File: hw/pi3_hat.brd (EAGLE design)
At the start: 56.5 x 65 mm, 109 parts, among them J1 XT30P, J2 XT30P, U1 AP64351SO8EP, U10 CAT24C32SOIC8, U11 STM32G474CEU6, U12 TCAN334GSOT23, U13 TCAN334GSOT23, U2 DMMT5401, U3 DMG2305UX, U4 STM32G474CEU6, U5 TCAN334GSOT23, U6 TCAN334GSOT23, U7 STM32G474CEU6, U8 BMI088LGA16, U9 TCAN334GSOT23

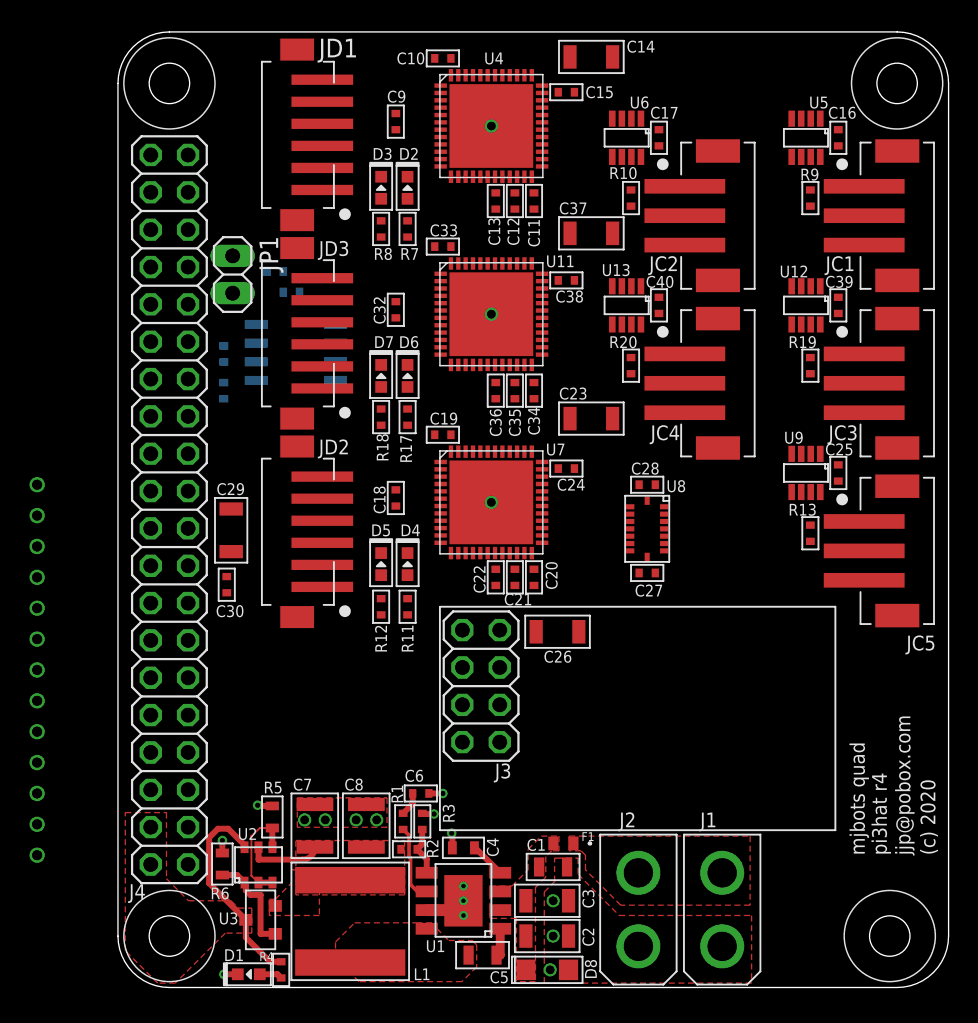
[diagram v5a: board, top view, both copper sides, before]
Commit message: Route all power and place all test points
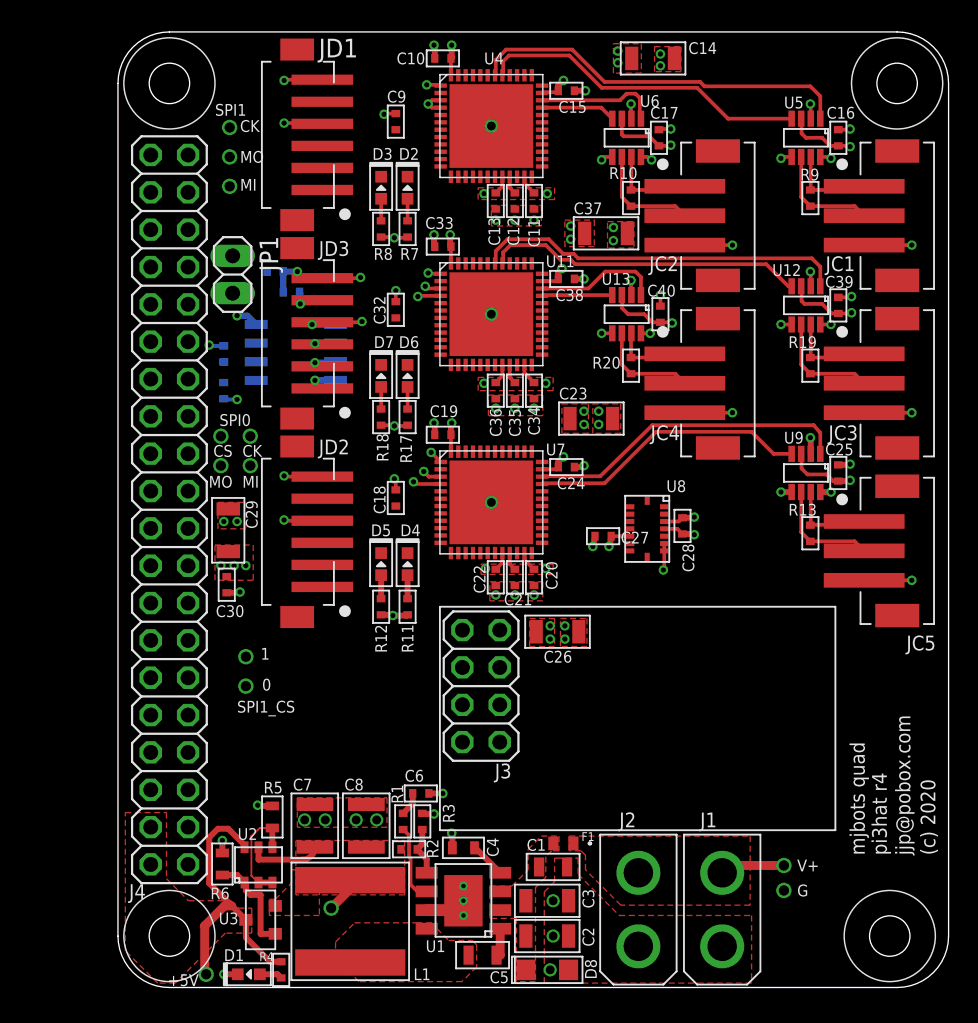
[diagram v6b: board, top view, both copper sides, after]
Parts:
- moved V+ 56.1 mm to (45.3, 8.30)
- moved GND 55.1 mm to (45.3, 6.60)
- moved SPI1_MOSI 41.2 mm to (7.60, 56.5)
- moved SPI1_SCLK 39.2 mm to (7.60, 58.5)
- moved SPI1_MISO 37.4 mm to (7.60, 54.5)
- moved REGOUT 35.1 mm to (14.5, 5.40)
- moved +5V 31.3 mm to (6.00, 0.90)
- moved SPI0_MOSI 29.3 mm to (7.00, 35.5)
- moved SPI0_MISO 28.4 mm to (9.00, 35.5)
- moved SPI0_SCLK 28.3 mm to (9.00, 37.5)
- moved SPI0_CS0 25.5 mm to (7.00, 37.5)
- moved SPI1_CS0 15.2 mm to (8.70, 20.5)
- moved SPI1_CS1 14.3 mm to (8.70, 22.5)
- moved C14 4.20 mm to (36.4, 63.2)
- moved C27 3.91 mm to (33.0, 30.7), turned to 180 degrees
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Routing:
- net +3V3: track 0.00 -> 76.9 mm, vias 0 -> 45
- net GND: track 8.48 -> 73.6 mm, vias 16 -> 84
- net N$18: track 0.00 -> 26.3 mm
- net N$42: track 0.00 -> 25.4 mm
- net N$17: track 0.00 -> 22.5 mm
- net N$55: track 0.00 -> 22.0 mm
- net N$41: track 0.00 -> 21.8 mm
- net N$54: track 0.00 -> 19.1 mm
- net N$40: track 0.00 -> 8.58 mm
- net N$100: track 0.00 -> 8.39 mm
- net N$8: track 0.00 -> 7.54 mm
- net N$46: track 0.00 -> 7.54 mm
- net N$4: track 0.00 -> 7.54 mm
- net N$25: track 0.00 -> 7.54 mm
- net N$27: track 0.00 -> 6.94 mm
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- added copper zone on layer 1, net +3V3
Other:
- board text added: "+5V"
- board text added: "0"
- board text added: "1"
- board text added: "CK"
- board text added: "CS"
- board text added: "G"
- board text added: "MI"
- board text added: "MO"
- board text added: "REGOUT"
- board text added: "SPI0"
- board text added: "SPI1"
- board text added: "SPI1_CS"
- board text added: "V+"

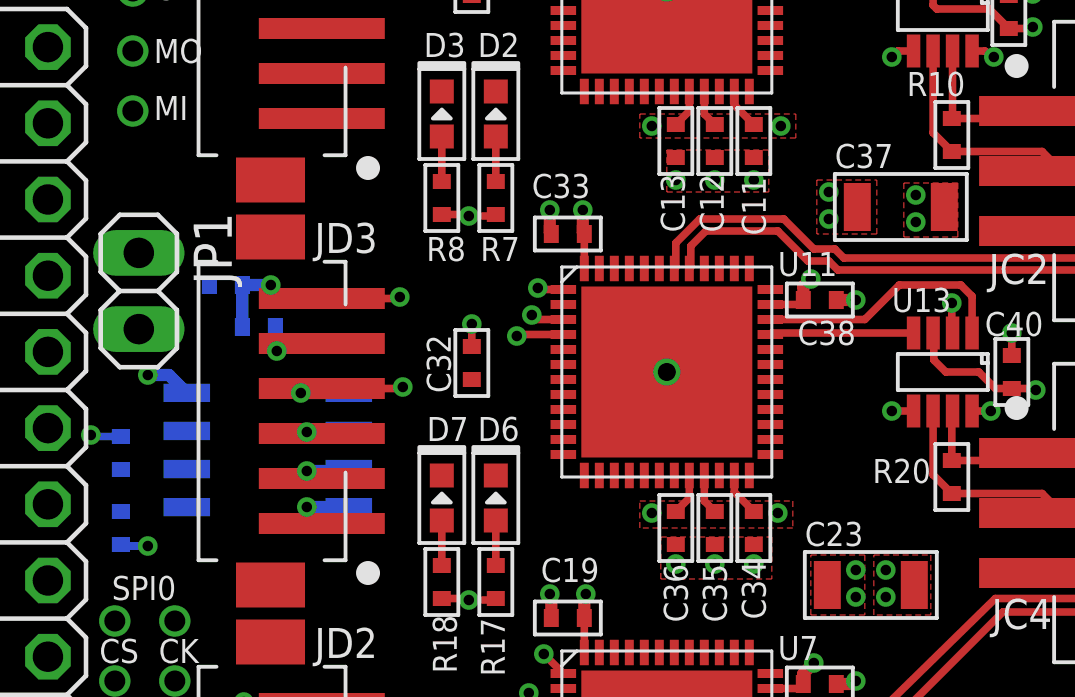
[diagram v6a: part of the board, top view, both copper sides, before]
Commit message: Fix enough things that the board with autoroute
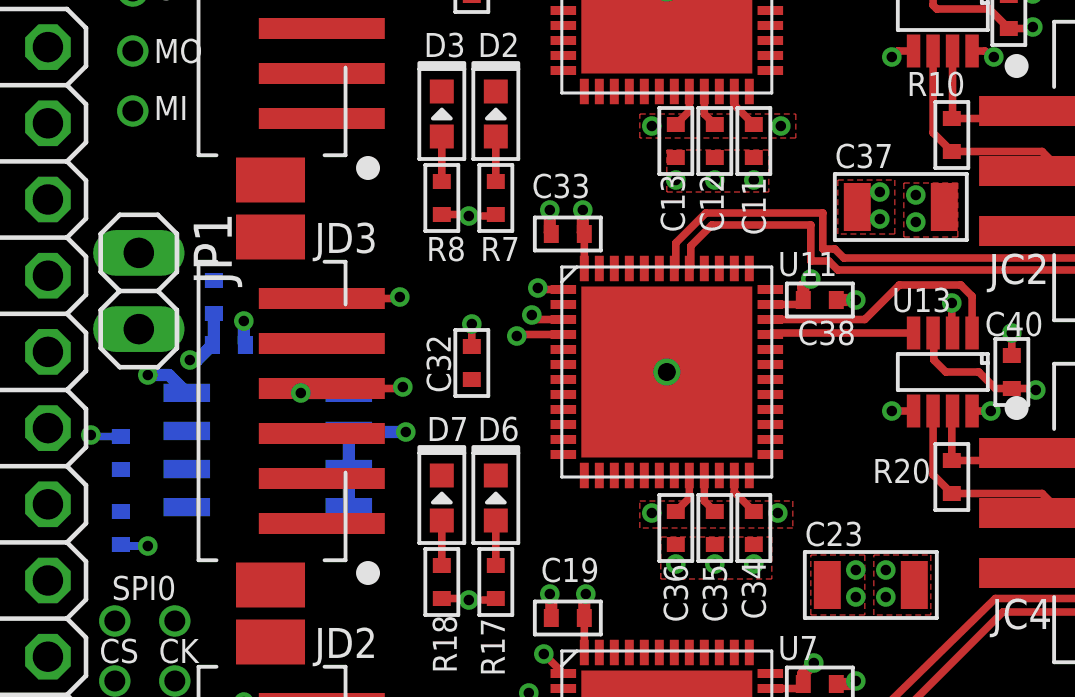
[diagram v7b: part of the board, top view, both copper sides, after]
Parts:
- moved C31 1.17 mm to (10.8, 46.7)
- moved R14 0.57 mm to (10.3, 48.3), turned to 90 degrees
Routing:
- net N$42: track 25.4 -> 26.2 mm
- net N$41: track 21.8 -> 22.6 mm
- net GND: track 73.6 -> 74.0 mm, vias 84 -> 82

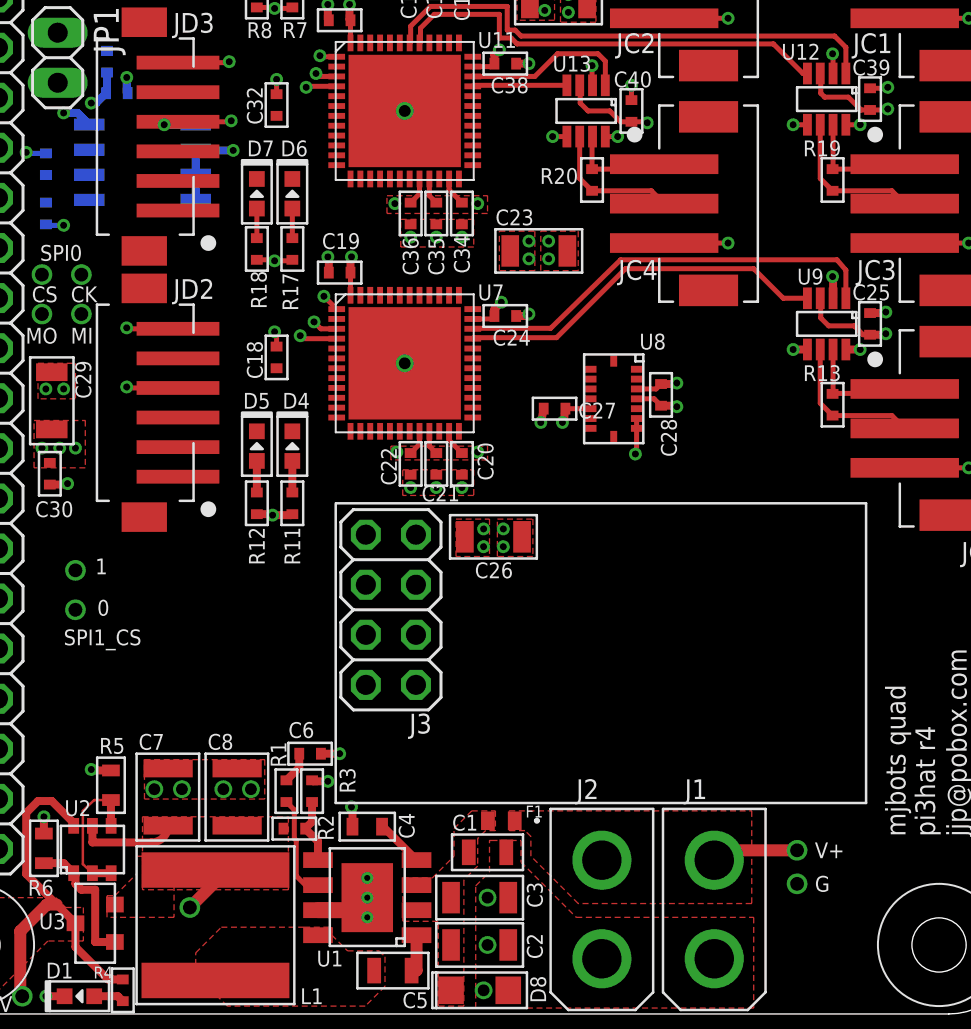
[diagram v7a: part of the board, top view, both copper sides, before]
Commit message: More fiddling, and add a 3.3v test point
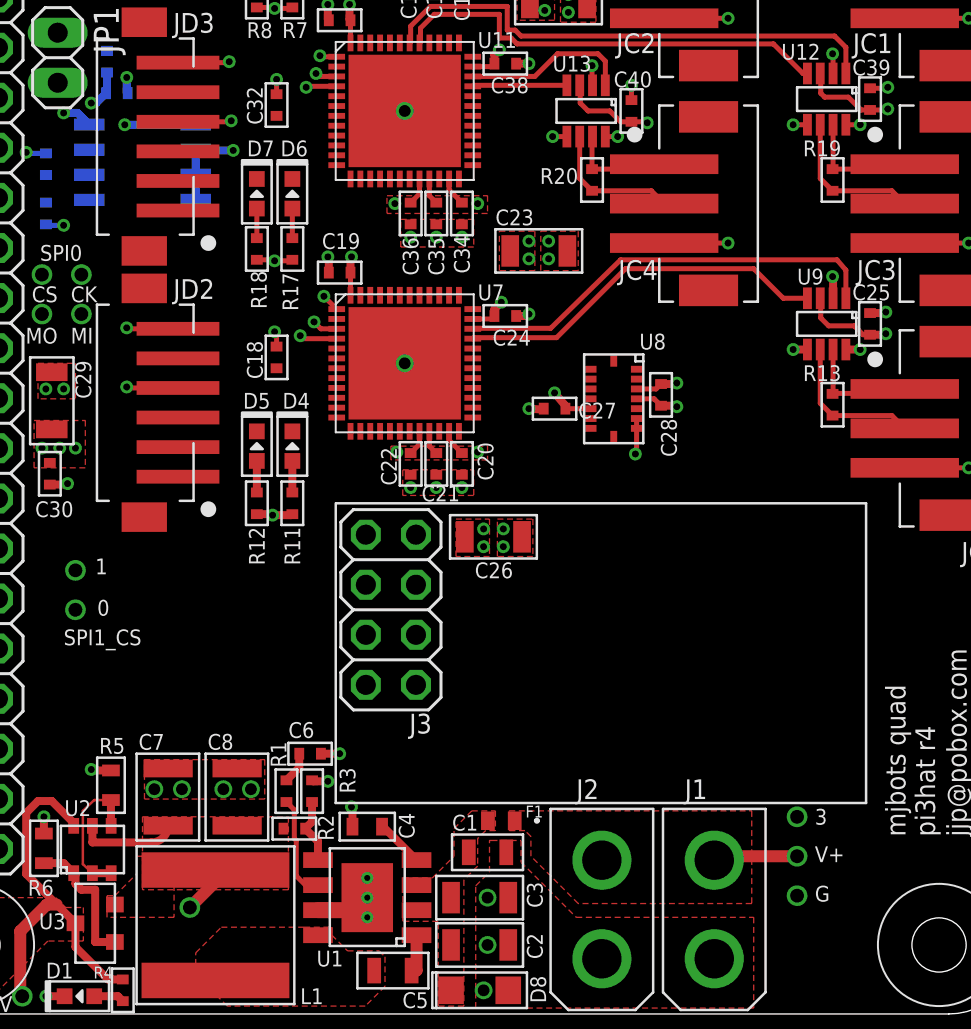
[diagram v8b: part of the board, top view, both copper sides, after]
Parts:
- added 3V3_TP: PAD24AWG_PAD, pi3_hat:24AWG_PAD
- moved GND 0.60 mm to (45.3, 6.00)
- moved V+ 0.30 mm to (45.3, 8.00)
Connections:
- net +3V3: now also 3V3_TP.P$1
- net IMU_ACC_INT: now also U7.32; no longer U7.30
- net IMU_CS1: now also U7.31; no longer U7.25
- net IMU_CS2: now also U7.25; no longer U7.24
- net IMU_GYRO_INT: now also U7.30; no longer U7.31
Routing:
- net GND: track 74.0 -> 76.1 mm
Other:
- board text added: "3"
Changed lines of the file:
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@@
 <layers>
 <layer number="1" name="Top" color="4" fill="1" visible="yes" active="yes"/>
-<layer number="2" name="Route2" color="1" fill="3" visible="yes" active="yes"/>
+<layer number="2" name="Route2" color="1" fill="3" visible="no" active="yes"/>
 <layer number="3" name="Route3" color="4" fill="3" visible="no" active="no"/>
 <layer number="4" name="Route4" color="1" fill="4" visible="no" active="no"/>
@@
 <layer number="13" name="Route13" color="4" fill="5" visible="no" active="no"/>
 <layer number="14" name="Route14" color="1" fill="6" visible="no" active="no"/>
-<layer number="15" name="Route15" color="4" fill="6" visible="yes" active="yes"/>
+<layer number="15" name="Route15" color="4" fill="6" visible="no" active="yes"/>
 <layer number="16" name="Bottom" color="1" fill="1" visible="yes" active="yes"/>
 <layer number="17" name="Pads" color="2" fill="1" visible="yes" active="yes"/>
@@
 <circle x="3.5" y="61.5" radius="3.1" width="0.1" layer="21"/>
 <text x="14.9" y="5.8" size="0.8" layer="26" rot="MR180">REGOUT</text>
-<text x="46.2" y="7.9" size="0.8" layer="25" font="vector">V+</text>
-<text x="46.2" y="6.2" size="0.8" layer="25" font="vector">G</text>
+<text x="46.2" y="7.7" size="0.8" layer="25" font="vector">V+</text>
+<text x="46.2" y="5.7" size="0.8" layer="25" font="vector">G</text>
 <text x="5.5" y="0.9" size="0.8" layer="25" font="vector" rot="R180">+5V</text>
 <text x="8.1" y="18.7" size="0.8" layer="25" font="vector">SPI1_CS</text>
@@
 <text x="7.8" y="34.8" size="0.8" layer="25" font="vector" rot="R180">MO</text>
 <text x="9.6" y="34.8" size="0.8" layer="25" font="vector" rot="R180">MI</text>
+<text x="46.2" y="9.6" size="0.8" layer="25" font="vector">3</text>
 </plain>
 <attributes>
@@
 </element>
 <element name="REGOUT" library="pi3_hat" package="24AWG_PAD" value="PAD24AWG_PAD" x="14.5" y="5.4"/>
-<element name="V+" library="pi3_hat" package="24AWG_PAD" value="PAD24AWG_PAD" x="45.3" y="8.3"/>
+<element name="V+" library="pi3_hat" package="24AWG_PAD" value="PAD24AWG_PAD" x="45.3" y="8"/>
 <element name="+5V" library="pi3_hat" package="24AWG_PAD" value="PAD24AWG_PAD" x="6" y="0.9"/>
-<element name="GND" library="pi3_hat" package="24AWG_PAD" value="PAD24AWG_PAD" x="45.3" y="6.6"/>
+<element name="GND" library="pi3_hat" package="24AWG_PAD" value="PAD24AWG_PAD" x="45.3" y="6"/>
 <element name="SPI1_CS0" library="pi3_hat" package="24AWG_PAD" value="PAD24AWG_PAD" x="8.7" y="20.5"/>
 <element name="SPI1_CS1" library="pi3_hat" package="24AWG_PAD" value="PAD24AWG_PAD" x="8.7" y="22.5"/>
@@
 <attribute name="NAME" x="31.77" y="1.94" size="0.8" layer="21" font="vector" ratio="10" rot="R270"/>
 </element>
+<element name="3V3_TP" library="pi3_hat" package="24AWG_PAD" value="PAD24AWG_PAD" x="45.3" y="10"/>
 </elements>
 <signals>
@@
 <wire x1="37.16" y1="31.2" x2="38.05" y2="31.2" width="0.254" layer="1"/>
 <wire x1="38.05" y1="31.2" x2="38.4" y2="30.85" width="0.254" layer="1"/>
-<via x="32.3" y="30" extent="1-16" drill="0.35"/>
+<via x="31.7" y="30.7" extent="1-16" drill="0.35"/>
 <wire x1="32.45" y1="30.7" x2="32.45" y2="30.65" width="0.4064" layer="1"/>
-<wire x1="32.45" y1="30.65" x2="32.3" y2="30" width="0.4064" layer="1"/>
+<wire x1="32.45" y1="30.65" x2="31.7" y2="30.7" width="0.4064" layer="1"/>
 <via x="41.8" y="39.1" extent="1-16" drill="0.35"/>
 <wire x1="38.56" y1="39.1" x2="41.8" y2="39.1" width="0.254" layer="1"/>
@@
 <wire x1="8.25" y1="26.85" x2="8.3" y2="26.9" width="0.4064" layer="1"/>
 <via x="11.3" y="47.5" extent="1-16" drill="0.35"/>
-<via x="13.2" y="45.1" extent="1-16" drill="0.35"/>
+<via x="11.2" y="45.1" extent="1-16" drill="0.35"/>
 <wire x1="14.8" y1="45.105" x2="14.795" y2="45.1" width="0.4064" layer="16"/>
-<wire x1="14.795" y1="45.1" x2="13.2" y2="45.1" width="0.4064" layer="16"/>
+<wire x1="14.795" y1="45.1" x2="11.2" y2="45.1" width="0.4064" layer="16"/>
 <wire x1="14.8" y1="41.295" x2="14.795" y2="41.3" width="0.4064" layer="16"/>
 <via x="16.7" y="43.8" extent="1-16" drill="0.35"/>
@@
 <wire x1="37.16" y1="31.7" x2="38.15" y2="31.7" width="0.254" layer="1"/>
 <wire x1="38.15" y1="31.7" x2="38.4" y2="31.95" width="0.254" layer="1"/>
-<via x="33.4" y="30" extent="1-16" drill="0.35"/>
-<wire x1="33.55" y1="30.7" x2="33.45" y2="29.95" width="0.4064" layer="1"/>
-<wire x1="33.45" y1="29.95" x2="33.4" y2="30" width="0.4064" layer="1"/>
+<via x="33" y="31.5" extent="1-16" drill="0.35"/>
+<wire x1="33.55" y1="30.7" x2="33.55" y2="30.85" width="0.4064" layer="1"/>
+<wire x1="33.55" y1="30.85" x2="33" y2="31.5" width="0.4064" layer="1"/>
 <wire x1="33.55" y1="30.7" x2="34.84" y2="30.7" width="0.254" layer="1"/>
 <via x="49.8" y="34.5" extent="1-16" drill="0.35"/>
@@
 <wire x1="10.25" y1="46.7" x2="10.3" y2="46.75" width="0.4064" layer="16"/>
 <wire x1="10.3" y1="46.75" x2="10.3" y2="47.75" width="0.4064" layer="16"/>
+<contactref element="3V3_TP" pad="P$1"/>
 </signal>
 <signal name="PI_TX_3V">
@@
 <vertex x="30.7" y="9.3"/>
 </polygon>
-<wire x1="41.1" y1="7.8" x2="41.6" y2="8.3" width="0.6096" layer="1"/>
-<wire x1="41.6" y1="8.3" x2="45.3" y2="8.3" width="0.6096" layer="1"/>
+<wire x1="41.1" y1="7.8" x2="41.3" y2="8" width="0.6096" layer="1"/>
+<wire x1="41.3" y1="8" x2="45.3" y2="8" width="0.6096" layer="1"/>
 </signal>
 <signal name="V+FUSED">
@@
 <signal name="IMU_CS1">
 <contactref element="U8" pad="14"/>
-<contactref element="U7" pad="25"/>
-<wire x1="28.85" y1="30.25" x2="34.84" y2="32.2" width="0" layer="19" extent="1-1"/>
+<contactref element="U7" pad="31"/>
+<wire x1="28.85" y1="33.25" x2="34.84" y2="32.2" width="0" layer="19" extent="1-1"/>
 </signal>
 <signal name="IMU_CS2">
 <contactref element="U8" pad="5"/>
-<contactref element="U7" pad="24"/>
-<wire x1="28.15" y1="29.55" x2="37.16" y2="30.7" width="0" layer="19" extent="1-1"/>
+<contactref element="U7" pad="25"/>
+<wire x1="28.85" y1="30.25" x2="37.16" y2="30.7" width="0" layer="19" extent="1-1"/>
 </signal>
 <signal name="IMU_ACC_INT">
 <contactref element="U8" pad="16"/>
-<contactref element="U7" pad="30"/>
-<wire x1="28.85" y1="32.75" x2="36" y2="33.115" width="0" layer="19" extent="1-1"/>
+<contactref element="U7" pad="32"/>
+<wire x1="28.85" y1="33.75" x2="36" y2="33.115" width="0" layer="19" extent="1-1"/>
 </signal>
 <signal name="IMU_GYRO_INT">
 <contactref element="U8" pad="12"/>
-<contactref element="U7" pad="31"/>
-<wire x1="28.85" y1="33.25" x2="34.84" y2="31.2" width="0" layer="19" extent="1-1"/>
+<contactref element="U7" pad="30"/>
+<wire x1="28.85" y1="32.75" x2="34.84" y2="31.2" width="0" layer="19" extent="1-1"/>
 </signal>
 <signal name="NRF_SCK">
